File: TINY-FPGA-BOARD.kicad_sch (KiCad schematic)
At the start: 20 parts, among them SW2 RST, U1 ICE40HX8K-BG121, U2 W25Q128JVS

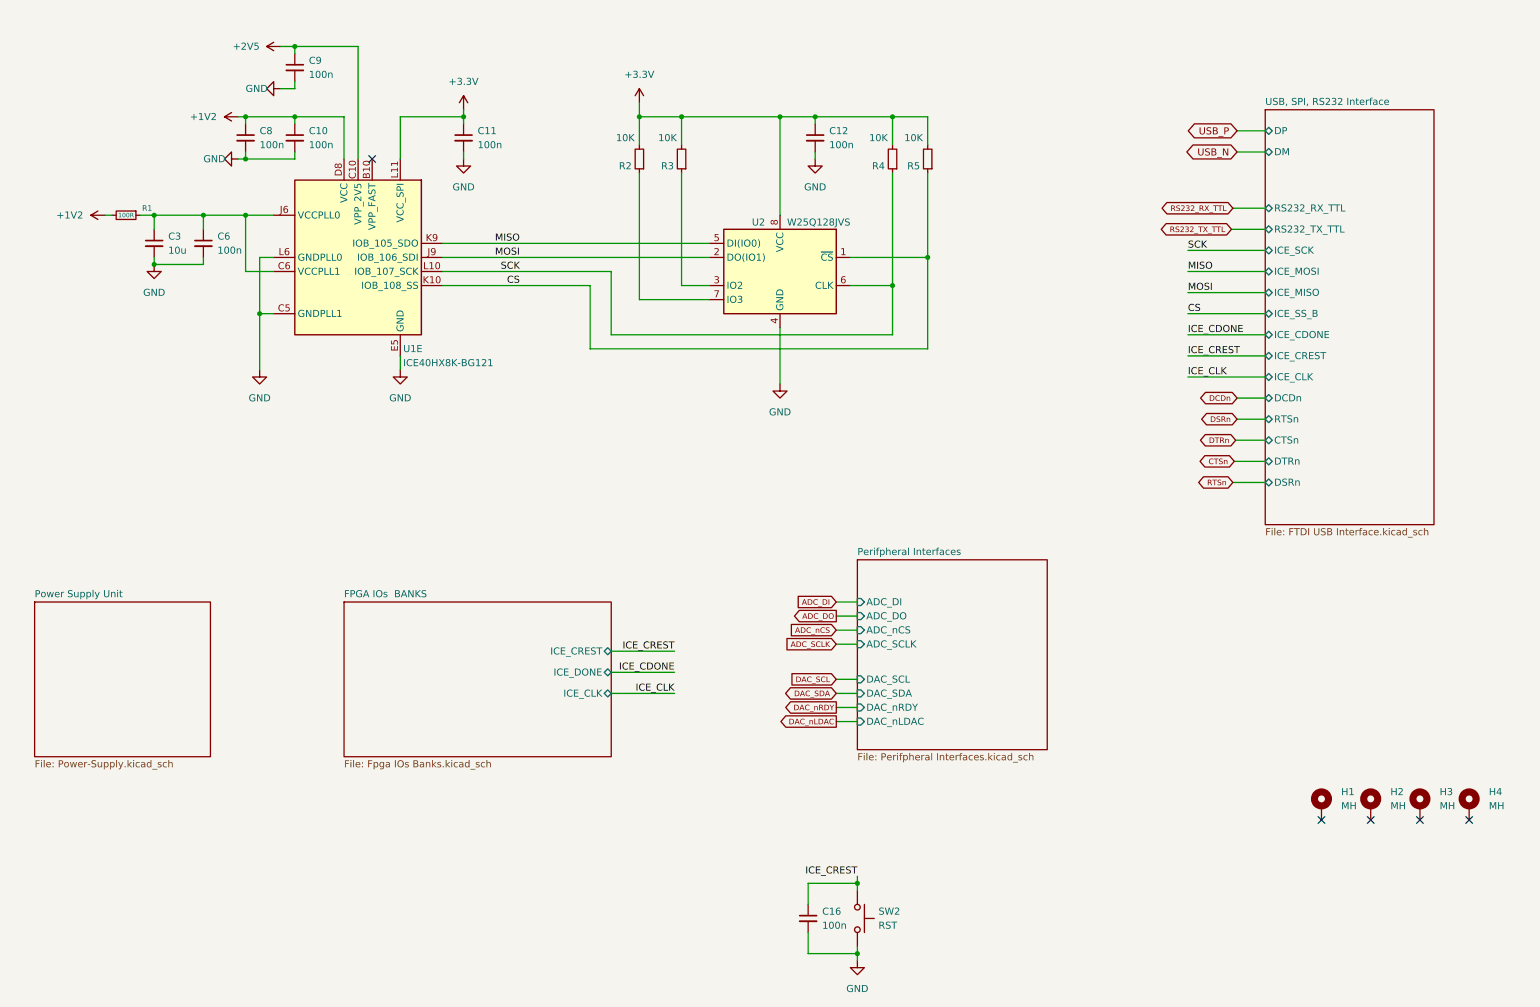
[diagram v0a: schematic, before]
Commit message: Update the description
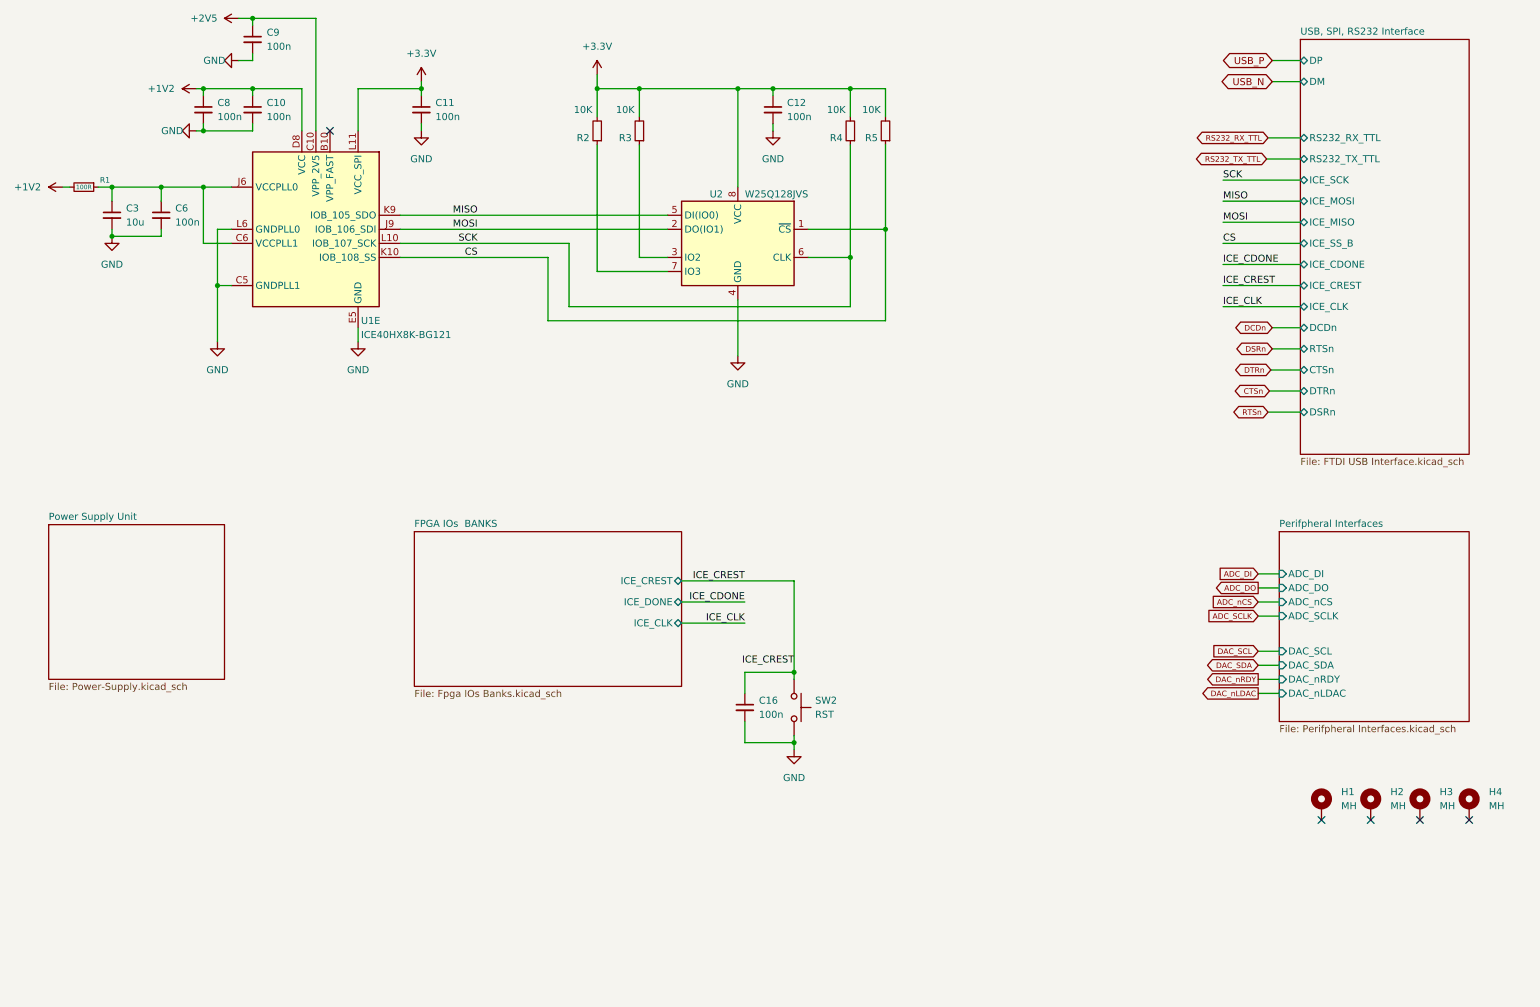
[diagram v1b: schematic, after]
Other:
- moved on the sheet: C10, C11, C12, C16, C3, C6, C8, C9, R1, R2, R3, R4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
